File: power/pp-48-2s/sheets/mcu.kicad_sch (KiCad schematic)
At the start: 20 parts, among them J5 SWD, U3 STM32G0B1CBT6, Y1 8MHz

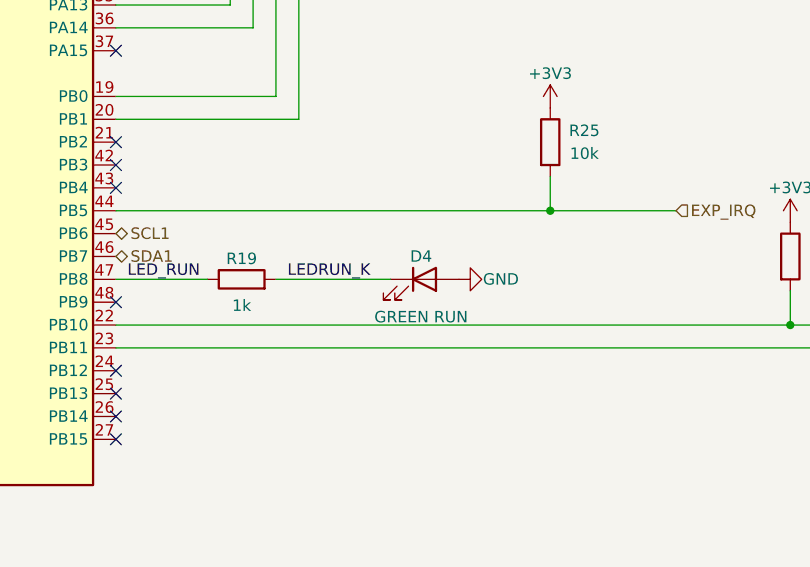
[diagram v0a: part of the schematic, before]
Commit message: power: PP-48-2S four fixes: LED polarity, LM5164 ripple network, latch clear driver, brick sense checked
LEDs: Device:LED pin 1 is K; every LED had the resistor on pin 1 and
GND on pin 2. Nets swapped (LEDnn_K -> LEDnn_A), footprints turned 180
degrees (plan 80). Ripple injection: TI SNVSAU4D Table 6-1 / Fig 7-1
have CA node -> VOUT and CB node -> FB; tables fixed, C5/C6 and
C12/C13 swapped places and rewired on the board (plans 81, 82). Latch
clear: Sn_LCLR now drives the Q104/Q204 gate (+ R112/R212); the latch
node is /Slot n/CLRN (plans 81, 83). Brick SENSE+/-: the PM-19V-200W
module leaves pins 5-7 unconnected, X1.5/X1.7 stay NC.
ERC 0; schcheck shows exactly the intended pin changes; board relinked
with pcbkit relink --allow-shorts and hand-fixed; gndpour, silk,
connlabels re-run; DRC 5 warnings as before, 0 unconnected.
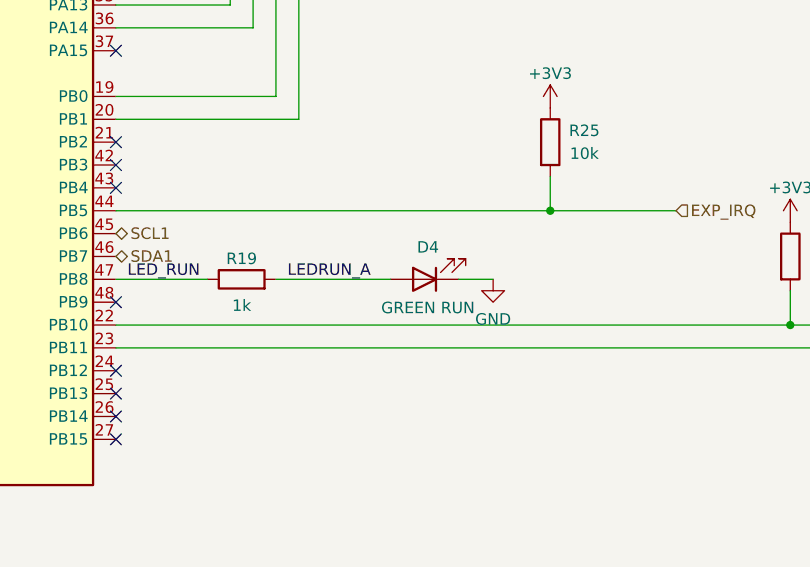
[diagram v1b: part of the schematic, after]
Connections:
- net GND: now also D4.1 (K); no longer D4.2 (A)
- net LEDRUN_K renamed LEDRUN_A
- net LEDRUN_A: now also D4.2 (A); no longer D4.1 (K)
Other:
- moved on the sheet: D4
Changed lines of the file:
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@@
 	(wire
 		(pts
+			(xy 269.24 187.96) (xy 273.05 187.96)
+		)
+		(stroke
+			(width 0)
+			(type default)
+		)
+	)
+	(wire
+		(pts
 			(xy 231.14 180.34) (xy 279.4 180.34)
 		)
@@
 		)
 	)
-	(label "LEDRUN_K"
+	(label "LEDRUN_A"
 		(at 250.19 187.96 0)
 		(effects
@@
 	(symbol
 		(lib_id "Device:LED")
-		(at 265.43 187.96 0)
+		(at 265.43 187.96 180)
 		(unit 1)
 		(body_style 1)
@@
 		(dnp no)
 		(property "Reference" "D4"
-			(at 265.049 185.42 0)
+			(at 265.811 184.404 0)
 			(show_name no)
 			(do_not_autoplace no)
@@
 		)
 		(property "Value" "GREEN RUN"
-			(at 265.049 192.151 0)
+			(at 265.811 191.135 0)
 			(show_name no)
 			(do_not_autoplace no)
@@
 	(symbol
 		(lib_id "power:GND")
-		(at 203.2 213.36 0)
+		(at 273.05 187.96 0)
 		(unit 1)
 		(body_style 1)
@@
 		(dnp no)
 		(property "Reference" "#PWR3011"
-			(at 203.2 213.36 0)
+			(at 273.05 187.96 0)
 			(hide yes)
 			(show_name no)
@@
 		)
 		(property "Value" "GND"
-			(at 203.2 217.805 0)
+			(at 273.05 192.405 0)
 			(show_name no)
 			(do_not_autoplace no)
@@
 		)
 		(property "Footprint" ""
-			(at 203.2 213.36 0)
+			(at 273.05 187.96 0)
 			(hide yes)
 			(show_name no)
@@
 		)
 		(property "Datasheet" ""
-			(at 203.2 213.36 0)
+			(at 273.05 187.96 0)
 			(hide yes)
 			(show_name no)
@@
 		)
 		(property "Description" ""
-			(at 203.2 213.36 0)
+			(at 273.05 187.96 0)
 			(hide yes)
 			(show_name no)
@@
 	(symbol
 		(lib_id "power:GND")
-		(at 179.07 111.76 0)
+		(at 203.2 213.36 0)
 		(unit 1)
 		(body_style 1)
@@
 		(dnp no)
 		(property "Reference" "#PWR3012"
-			(at 179.07 111.76 0)
+			(at 203.2 213.36 0)
 			(hide yes)
 			(show_name no)
@@
 		)
 		(property "Value" "GND"
-			(at 179.07 116.205 0)
+			(at 203.2 217.805 0)
 			(show_name no)
 			(do_not_autoplace no)
@@
 		)
 		(property "Footprint" ""
-			(at 179.07 111.76 0)
+			(at 203.2 213.36 0)
 			(hide yes)
 			(show_name no)
@@
 		)
 		(property "Datasheet" ""
-			(at 179.07 111.76 0)
+			(at 203.2 213.36 0)
 			(hide yes)
 			(show_name no)
@@
 		)
 		(property "Description" ""
-			(at 179.07 111.76 0)
+			(at 203.2 213.36 0)
 			(hide yes)
 			(show_name no)
@@
 	(symbol
 		(lib_id "power:GND")
-		(at 190.5 111.76 0)
+		(at 179.07 111.76 0)
 		(unit 1)
 		(body_style 1)
@@
 		(dnp no)
 		(property "Reference" "#PWR3013"
-			(at 190.5 111.76 0)
+			(at 179.07 111.76 0)
 			(hide yes)
 			(show_name no)
@@
 		)
 		(property "Value" "GND"
-			(at 190.5 116.205 0)
+			(at 179.07 116.205 0)
 			(show_name no)
 			(do_not_autoplace no)
@@
 		)
 		(property "Footprint" ""
-			(at 190.5 111.76 0)
+			(at 179.07 111.76 0)
 			(hide yes)
 			(show_name no)
@@
 		)
 		(property "Datasheet" ""
-			(at 190.5 111.76 0)
+			(at 179.07 111.76 0)
 			(hide yes)
 			(show_name no)
@@
 		)
 		(property "Description" ""
-			(at 190.5 111.76 0)
+			(at 179.07 111.76 0)
 			(hide yes)
 			(show_name no)
@@
 	(symbol
 		(lib_id "power:GND")
-		(at 210.82 111.76 0)
+		(at 190.5 111.76 0)
 		(unit 1)
 		(body_style 1)
@@
 		(dnp no)
 		(property "Reference" "#PWR3014"
-			(at 210.82 111.76 0)
+			(at 190.5 111.76 0)
 			(hide yes)
 			(show_name no)
@@
 		)
 		(property "Value" "GND"
-			(at 210.82 116.205 0)
+			(at 190.5 116.205 0)
 			(show_name no)
 			(do_not_autoplace no)
@@
 		)
 		(property "Footprint" ""
-			(at 210.82 111.76 0)
+			(at 190.5 111.76 0)
 			(hide yes)
 			(show_name no)
@@
 		)
 		(property "Datasheet" ""
-			(at 210.82 111.76 0)
+			(at 190.5 111.76 0)
 			(hide yes)
 			(show_name no)
@@
 		)
 		(property "Description" ""
-			(at 210.82 111.76 0)
+			(at 190.5 111.76 0)
 			(hide yes)
 			(show_name no)
@@
 	(symbol
 		(lib_id "power:GND")
-		(at 162.56 121.92 0)
+		(at 210.82 111.76 0)
 		(unit 1)
 		(body_style 1)
@@
 		(dnp no)
 		(property "Reference" "#PWR3015"
-			(at 162.56 121.92 0)
+			(at 210.82 111.76 0)
 			(hide yes)
 			(show_name no)
@@
 		)
 		(property "Value" "GND"
-			(at 162.56 126.365 0)
+			(at 210.82 116.205 0)
 			(show_name no)
 			(do_not_autoplace no)
@@
 		)
 		(property "Footprint" ""
-			(at 162.56 121.92 0)
+			(at 210.82 111.76 0)
 			(hide yes)
 			(show_name no)
@@
 		)
 		(property "Datasheet" ""
-			(at 162.56 121.92 0)
+			(at 210.82 111.76 0)
 			(hide yes)
 			(show_name no)
@@
 		)
 		(property "Description" ""
-			(at 162.56 121.92 0)
+			(at 210.82 111.76 0)
 			(hide yes)
 			(show_name no)
@@
 	(symbol
 		(lib_id "power:GND")
-		(at 142.24 121.92 0)
+		(at 162.56 121.92 0)
 		(unit 1)
 		(body_style 1)
@@
 		(dnp no)
 		(property "Reference" "#PWR3016"
-			(at 142.24 121.92 0)
+			(at 162.56 121.92 0)
 			(hide yes)
 			(show_name no)
@@
 		)
 		(property "Value" "GND"
-			(at 142.24 126.365 0)
+			(at 162.56 126.365 0)
 			(show_name no)
 			(do_not_autoplace no)
@@
 		)
 		(property "Footprint" ""
-			(at 142.24 121.92 0)
+			(at 162.56 121.92 0)
 			(hide yes)
 			(show_name no)
@@
 		)
 		(property "Datasheet" ""
-			(at 142.24 121.92 0)
+			(at 162.56 121.92 0)
 			(hide yes)
 			(show_name no)
@@
 		)
 		(property "Description" ""
-			(at 142.24 121.92 0)
+			(at 162.56 121.92 0)
 			(hide yes)
 			(show_name no)
@@
 	(symbol
 		(lib_id "power:GND")
-		(at 152.4 144.78 0)
+		(at 142.24 121.92 0)
 		(unit 1)
 		(body_style 1)
@@
 		(dnp no)
 		(property "Reference" "#PWR3017"
-			(at 152.4 144.78 0)
+			(at 142.24 121.92 0)
 			(hide yes)
 			(show_name no)
@@
 		)
 		(property "Value" "GND"
-			(at 152.4 149.225 0)
+			(at 142.24 126.365 0)
 			(show_name no)
 			(do_not_autoplace no)
@@
 		)
 		(property "Footprint" ""
-			(at 152.4 144.78 0)
+			(at 142.24 121.92 0)
 			(hide yes)
 			(show_name no)
@@
 		)
 		(property "Datasheet" ""
-			(at 152.4 144.78 0)
+			(at 142.24 121.92 0)
 			(hide yes)
 			(show_name no)
@@
 		)
 		(property "Description" ""
-			(at 152.4 144.78 0)
+			(at 142.24 121.92 0)
 			(hide yes)
 			(show_name no)
@@
 	(symbol
 		(lib_id "power:GND")
-		(at 269.24 187.96 90)
+		(at 152.4 144.78 0)
 		(unit 1)
 		(body_style 1)
@@
 		(dnp no)
 		(property "Reference" "#PWR3018"
-			(at 269.24 187.96 90)
+			(at 152.4 144.78 0)
 			(hide yes)
 			(show_name no)
@@
 		)
 		(property "Value" "GND"
-			(at 273.915 187.96 90)
+			(at 152.4 149.225 0)
 			(show_name no)
 			(do_not_autoplace no)
@@
 		)
 		(property "Footprint" ""
-			(at 269.24 187.96 0)
+			(at 152.4 144.78 0)
 			(hide yes)
 			(show_name no)
@@
 		)
 		(property "Datasheet" ""
-			(at 269.24 187.96 0)
+			(at 152.4 144.78 0)
 			(hide yes)
 			(show_name no)
@@
 		)
 		(property "Description" ""
-			(at 269.24 187.96 0)
+			(at 152.4 144.78 0)
 			(hide yes)
 			(show_name no)

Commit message: power: PP-48-2S plane MCU STM32G0B1CBT6 -> STM32G070CBT6 (G0B1 out of stock at LCSC; pinout checked, 8-slot S7 pins moved off the unbonded 29/32); handoff: JLC stock check
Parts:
- U3: value STM32G0B1CBT6 -> STM32G070CBT6; symbol MCU_ST_STM32G0:STM32G0B1CBTx -> MCU_ST_STM32G0:STM32G070CBTx; LCSC C2847904 -> C529338
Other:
- moved on the sheet: C21, D4, R19, R23, R24, R25
